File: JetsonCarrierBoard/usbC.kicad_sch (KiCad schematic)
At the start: 4 parts

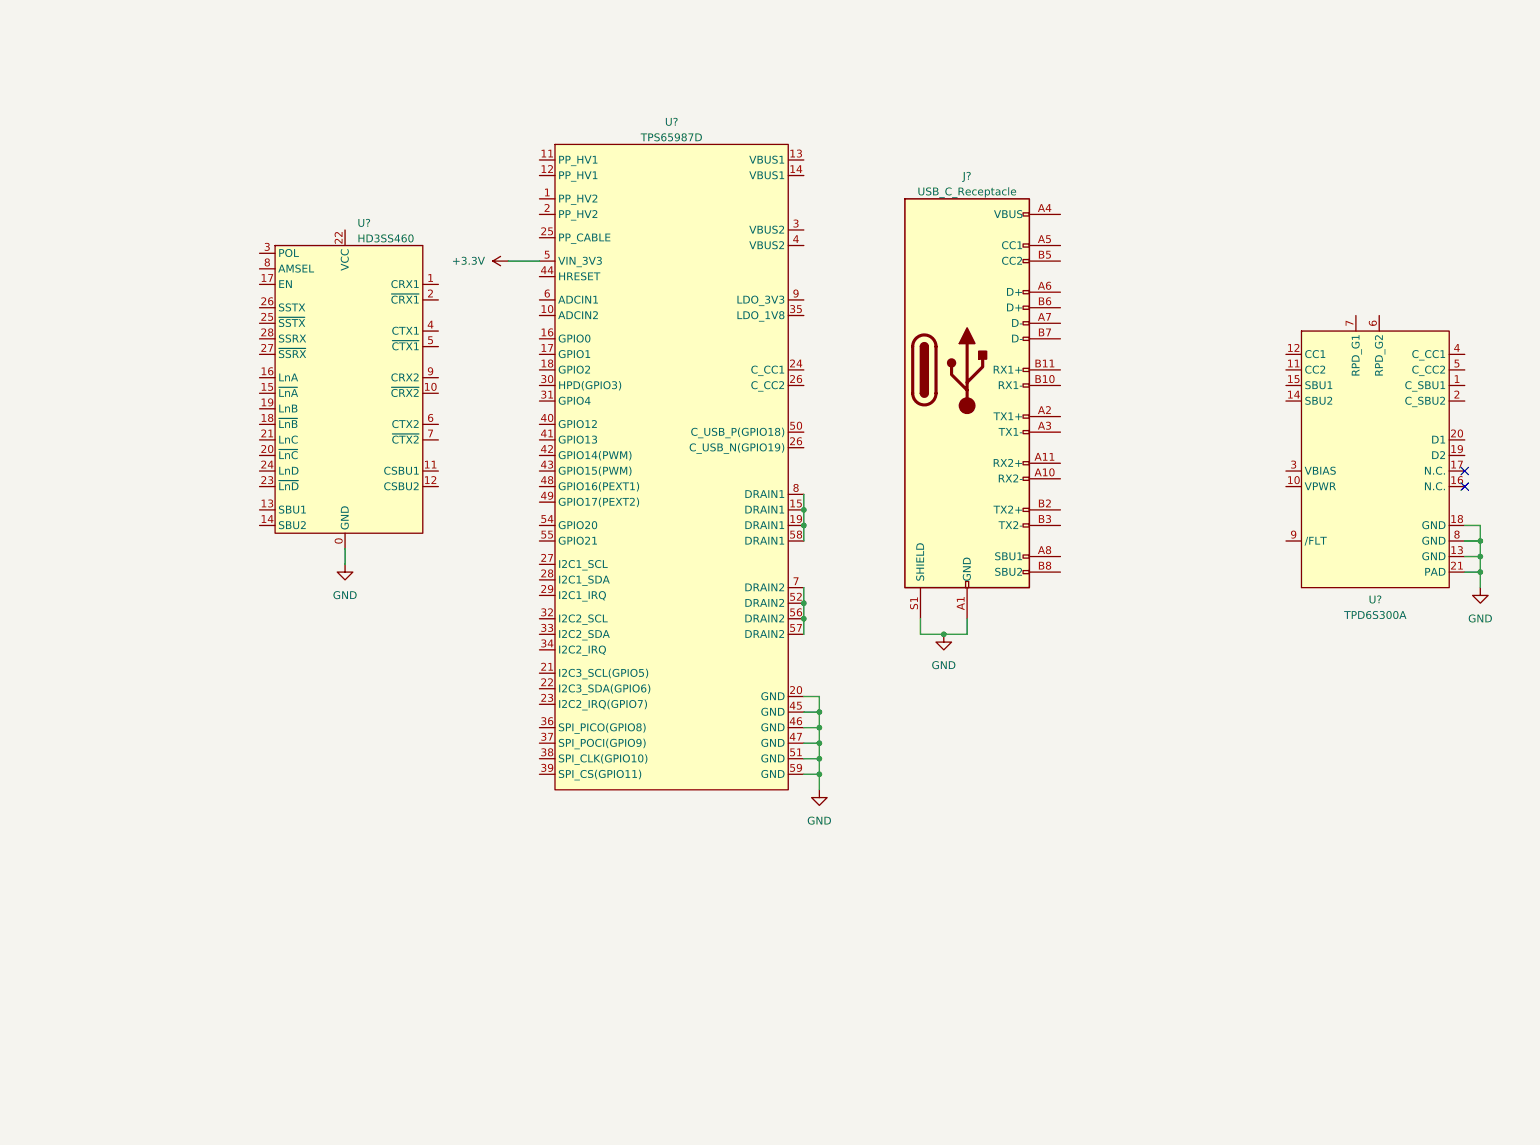
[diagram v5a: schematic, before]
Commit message: Part 2 of USB C wiring, renaming schematics
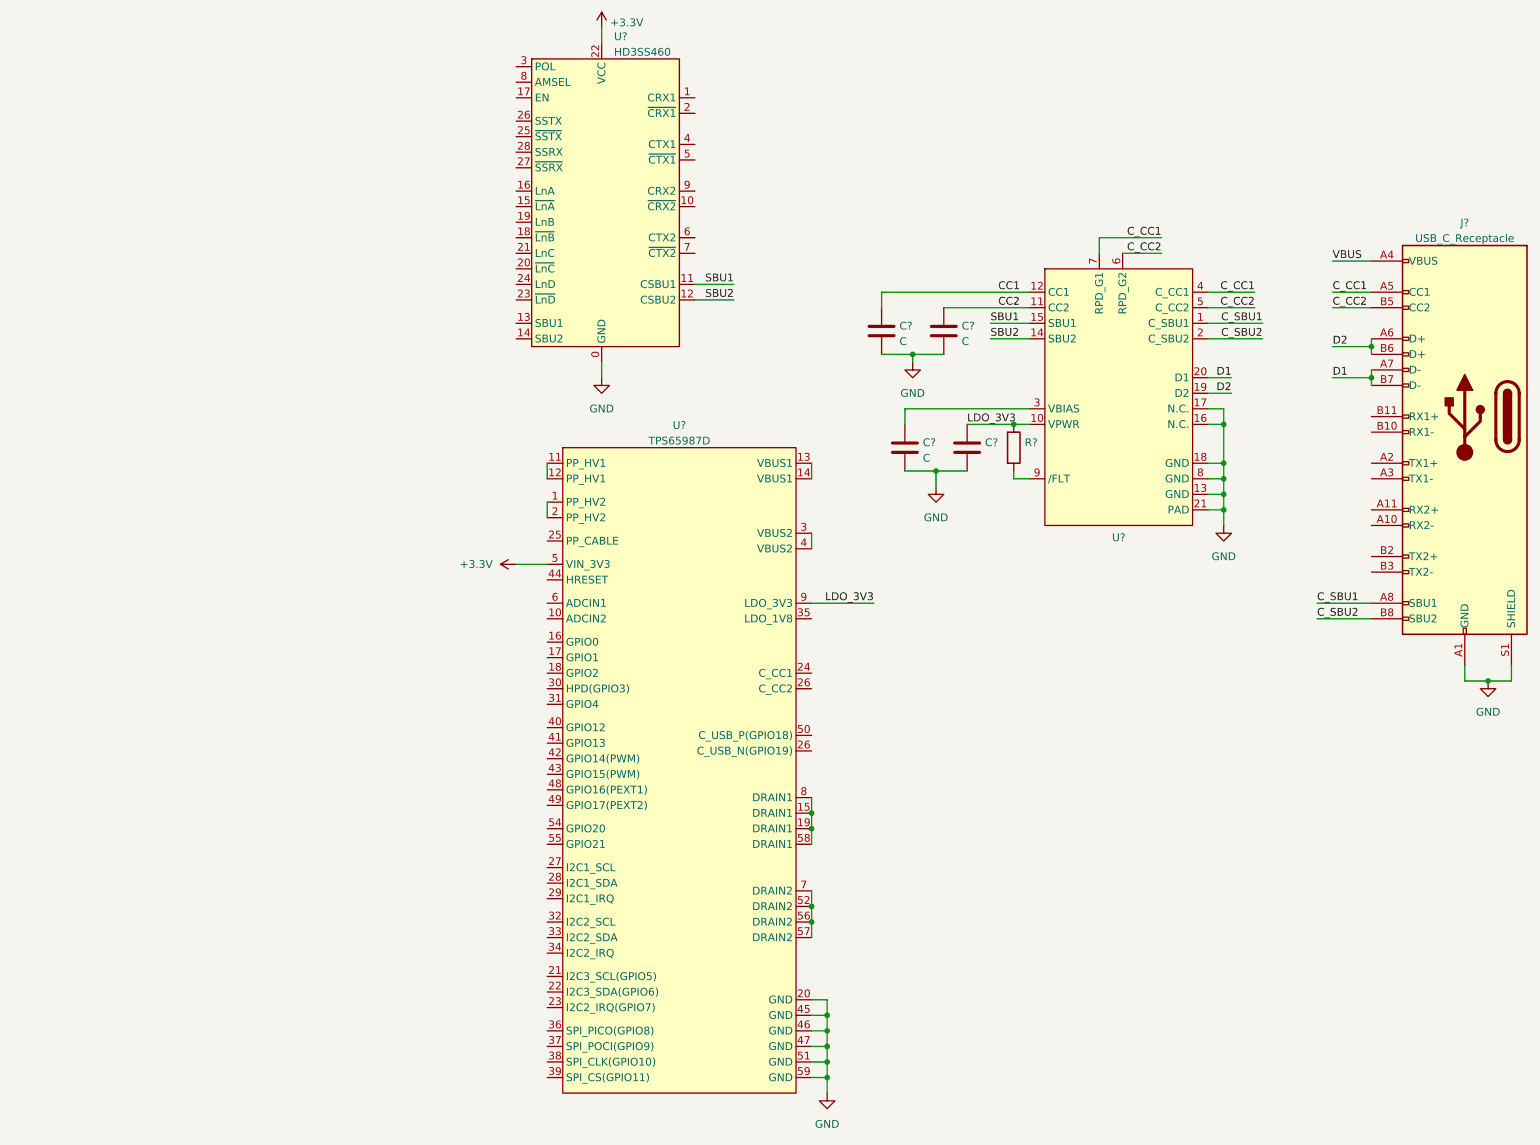
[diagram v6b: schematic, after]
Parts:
- added C? (x3): C, symbol Device:C
- added C?: (no value), symbol Device:C
- added R?: (no value), symbol Device:R
- U?: value TPD6S300A -> (none)
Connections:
- net +3.3V: now also U?.22 (VCC)
- net GND: now also U?.16 (N.C.), U?.17 (N.C.), C?.1, C?.1, C?.1, C?.1
- net at U?.1 (PP_HV2): now also U?.2 (PP_HV2)
- net at U?.11 (PP_HV1): now also U?.12 (PP_HV1)
- net at U?.13 (VBUS1): now also U?.14 (VBUS1)
- net at U?.3 (VBUS2): now also U?.4 (VBUS2)
- net LDO_3V3: now reaches U?.9 (LDO_3V3)
- net LDO_3V3: now also U?.10 (VPWR), C?.2, R?.1
- net C_SBU1: now reaches U?.1 (C_SBU1)
- net C_SBU1: now also J?.A8 (SBU1)
- net CC2: now reaches U?.11 (CC2)
- net CC2: now also C?.2
- net CC1: now reaches U?.12 (CC1)
- net CC1: now also C?.2
- net SBU2: now reaches U?.14 (SBU2)
- net SBU2: now also U?.12 (CSBU2)
- net SBU1: now reaches U?.15 (SBU1)
- net SBU1: now also U?.11 (CSBU1)
- net D2: now reaches U?.19 (D2)
- net D2: now also J?.A6 (D+), J?.B6 (D+)
- net C_SBU2: now reaches U?.2 (C_SBU2)
- net C_SBU2: now also J?.B8 (SBU2)
- net D1: now reaches U?.20 (D1)
- net D1: now also J?.A7 (D-), J?.B7 (D-)
- net at U?.3 (VBIAS): now also C?.2
- net C_CC1: now reaches U?.4 (C_CC1)
- net C_CC1: now also J?.A5 (CC1), U?.7 (RPD_G1)
- net C_CC2: now reaches U?.5 (C_CC2)
- net C_CC2: now also J?.B5 (CC2), U?.6 (RPD_G2)
- net at U?.9 (/FLT): now also R?.2
- net VBUS: now reaches J?.A4 (VBUS), J?.A9 (VBUS), J?.B4 (VBUS), J?.B9 (VBUS)
- no-connect marks 2 -> 0
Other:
- moved on the sheet: J?, U?

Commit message: Finished USB-C w/ Alt mode and PD Wiring V1
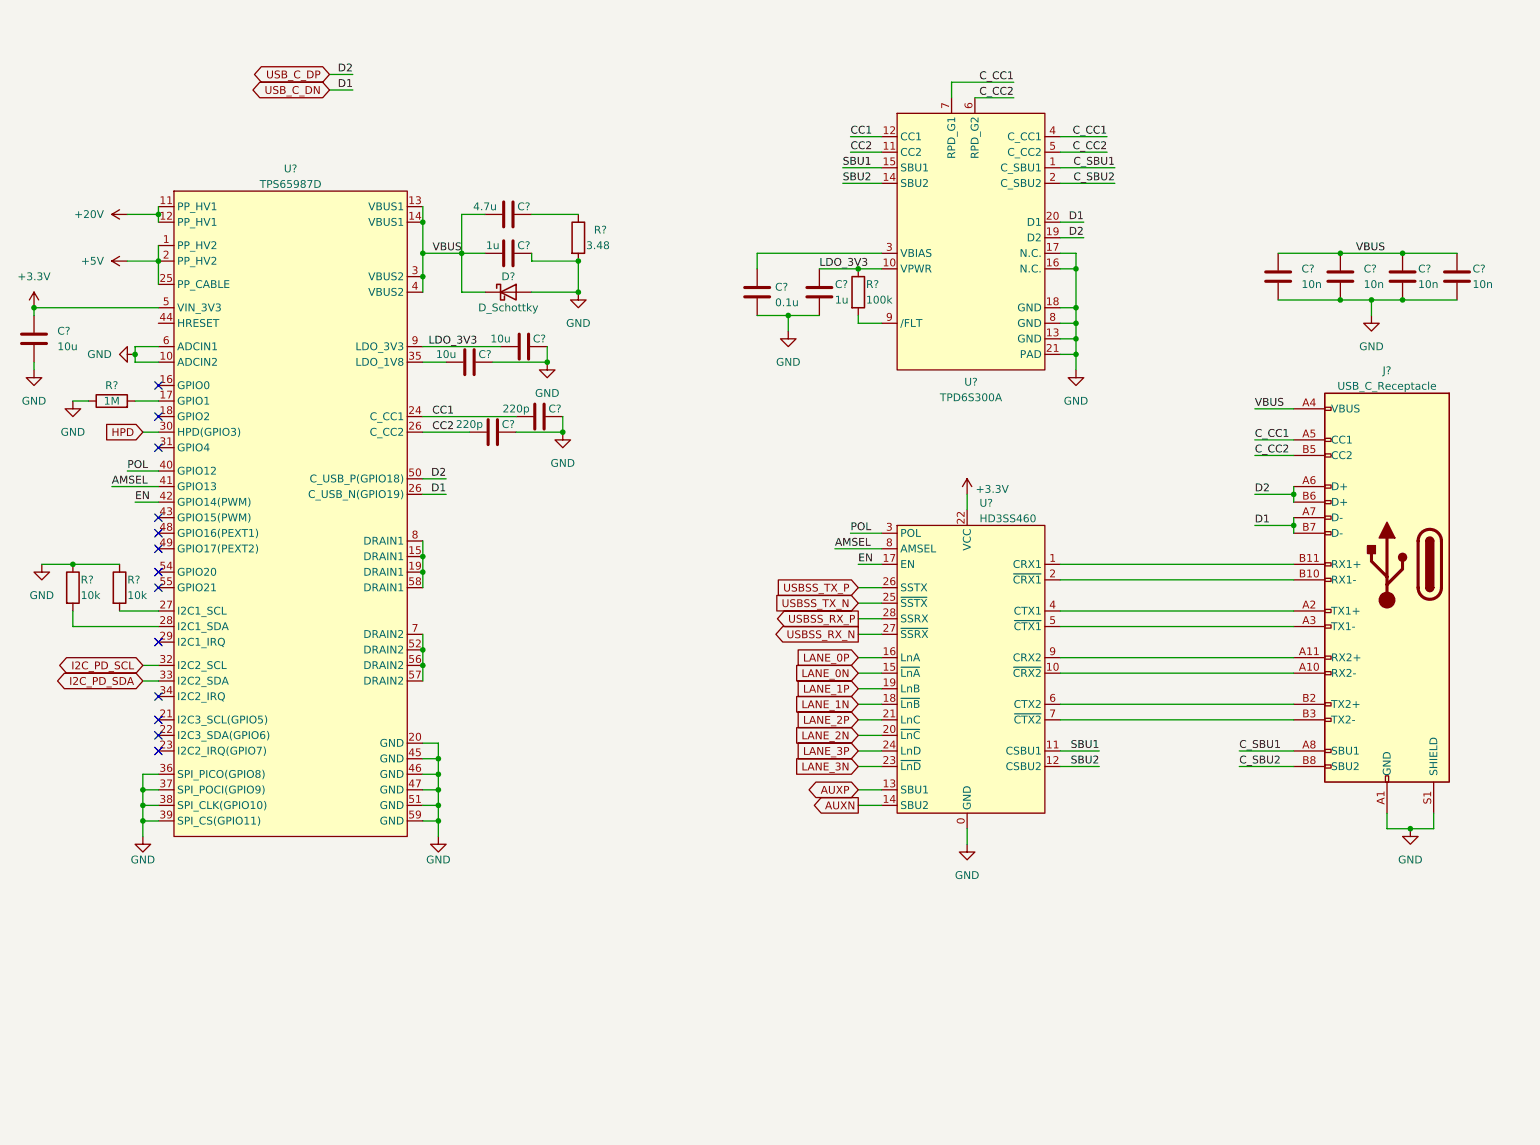
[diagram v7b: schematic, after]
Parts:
- removed C? (x2): C, symbol Device:C
- added C? (x3): 10u, symbol Device:C
- added C? (x4): 10n, symbol Device:C
- added C? (x2): 220p, symbol Device:C
- added C?: 1u, symbol Device:C
- added C?: 4.7u, symbol Device:C
- added D?: D_Schottky, symbol Device:D_Schottky
- added R? (x2): 10k, symbol Device:R
- added R?: 3.48, symbol Device:R
- added R?: 1M, symbol Device:R
- C?: value C -> 0.1u
- C?: value (none) -> 1u
- R?: value (none) -> 100k
- U?: value (none) -> TPD6S300A
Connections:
- net D1 is gone; now on net USB_C_DN: J?.A7 (D-), J?.B7 (D-), U?.20 (D1)
- net D2 is gone; now on net USB_C_DP: J?.A6 (D+), J?.B6 (D+), U?.19 (D2)
- net +3.3V: now also C?.2
- net CC1: now also U?.24 (C_CC1), C?.2
- net CC2: now also U?.26 (C_USB_N(GPIO19)), C?.2
- net GND: now also U?.10 (ADCIN2), U?.36 (SPI_PICO(GPIO8)), U?.37 (SPI_POCI(GPIO9)), U?.38 (SPI_CLK(GPIO10)), U?.39 (SPI_CS(GPIO11)), U?.6 (ADCIN1), C?.1, C?.1, C?.1, C?.1, C?.1, C?.1, C?.1, C?.1, C?.1, C?.1, D?.2 (A), R?.1, R?.1, R?.1, R?.2
- net LDO_3V3: now also C?.2
- net VBUS: now also U?.13 (VBUS1), U?.14 (VBUS1), U?.3 (VBUS2), U?.4 (VBUS2), C?.2, C?.2, C?.2, C?.2, C?.2, C?.2, D?.1 (K)
- net +5V: now reaches U?.1 (PP_HV2), U?.2 (PP_HV2)
- net +5V: now also U?.25 (PP_CABLE)
- net +20V: now reaches U?.11 (PP_HV1), U?.12 (PP_HV1)
- net at U?.17 (GPIO1): now also R?.2
- net USB_C_DN: now reaches U?.26 (C_USB_N(GPIO19))
- net at U?.27 (I2C1_SCL): now also R?.2
- net at U?.28 (I2C1_SDA): now also R?.2
- net HPD: now reaches U?.30 (HPD(GPIO3))
- net I2C_PD_SCL: now reaches U?.32 (I2C2_SCL)
- net I2C_PD_SDA: now reaches U?.33 (I2C2_SDA)
- net at U?.35 (LDO_1V8): now also C?.2
- net POL: now reaches U?.40 (GPIO12)
- net POL: now also U?.3 (POL)
- net AMSEL: now reaches U?.41 (GPIO13)
- net AMSEL: now also U?.8 (AMSEL)
- net EN: now reaches U?.42 (GPIO14(PWM))
- net EN: now also U?.17 (EN)
- net USB_C_DP: now reaches U?.50 (C_USB_P(GPIO18))
- net at J?.A10 (RX2-): now also U?.10 (~{CRX2})
- net at J?.A11 (RX2+): now also U?.9 (CRX2)
- net at J?.A2 (TX1+): now also U?.4 (CTX1)
- net at J?.A3 (TX1-): now also U?.5 (~{CTX1})
- net at J?.B10 (RX1-): now also U?.2 (~{CRX1})
- net at J?.B11 (RX1+): now also U?.1 (CRX1)
- net at J?.B2 (TX2+): now also U?.6 (CTX2)
- net at J?.B3 (TX2-): now also U?.7 (~{CTX2})
- net AUXP: now reaches U?.13 (SBU1)
- net AUXN: now reaches U?.14 (SBU2)
- net LANE_0N: now reaches U?.15 (~{LnA})
- net LANE_0P: now reaches U?.16 (LnA)
- net LANE_1N: now reaches U?.18 (~{LnB})
- net LANE_1P: now reaches U?.19 (LnB)
- net LANE_2N: now reaches U?.20 (~{LnC})
- net LANE_2P: now reaches U?.21 (LnC)
- net LANE_3N: now reaches U?.23 (~{LnD})
- net LANE_3P: now reaches U?.24 (LnD)
- net USBSS_TX_N: now reaches U?.25 (~{SSTX})
- net USBSS_TX_P: now reaches U?.26 (SSTX)
- net USBSS_RX_N: now reaches U?.27 (~{SSRX})
- net USBSS_RX_P: now reaches U?.28 (SSRX)
- new net: C?.1, R?.1
- no-connect marks 0 -> 13
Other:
- moved on the sheet: C?, J?, R?, U?
